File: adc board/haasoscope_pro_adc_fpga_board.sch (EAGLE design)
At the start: 582 parts, among them CN2 12Vin, IC1 ADC12DL2500ACF, IC10 TPS72325DBVR, IC13 LMH5401IRMST, IC14 LMH6401IRMZR, IC15 SN74AVC4T774PWR, IC17 DAC8562SDGSR, IC18 TLV9102IPWR, IC2 SN74AVC4T774PWR, IC21 LMH5401IRMST, IC22 TPS7A7200RGTR, IC23 TPS7A7200RGTR, IC24 TPS7A7200RGTR, IC25 TPS72325DBVR, IC26 TPS7A7200RGTR, IC27 TPS7A7200RGTR, IC28 TPS7A7200RGTR, IC29 LMH6401IRMZR, IC3 ADC122S021CIMM_NOPB, IC30 SN74AVC4T774PWR, IC33 TLV9102IPWR, IC4 TLV9102IPWR, IC5 EP4CE30F23C6N, IC6 EPCQ16ASI8N, IC7 TPS7A7200RGTR, IC8 FT232HQ, IC9 93LC56B, J1 2p-2.54, J10 8pin, J11 8pin, J13 8pin, J15 test1, J2 test1, J3 2p-2.54, J30 2p-2.54, J31 2p-2.54, J32 2p-2.54, J33 2p-2.54, J34 2p-2.54, J35 2p-2.54, J36 2p-2.54, J37 2p-2.54, J39 2p-2.54, J4 2p-2.54, J40 2p-2.54, J41 2p-2.54, J42 2p-2.54, J43 2p-2.54, J44 2p-2.54, J45 2p-2.54, J46 2p-2.54, J8 8pin, K1 G6K-2F-RF-T-TR03_DC5, K2 G6K-2F-RF-T-TR03_DC5, K3 G6K-2F-RF-T-TR03_DC5, K4 G6K-2F-RF-T-TR03_DC5, K5 G6K-2F-RF-T-TR03_DC5, K6 TLP3475R_TP,F, K7 TLP3475R_TP,F, Q1 S8050, Q2 FDN340P, Q4 S8050, Q5 S8050, Q7 S8050, Q8 S8050, Q9 S8050, SW3 SKQGADE010, SW4 SKQGADE010, U2 ADF4350BCPZ, X1 USBC, Y2 OSCILLATORSMD-5X3, Y3 12MHz

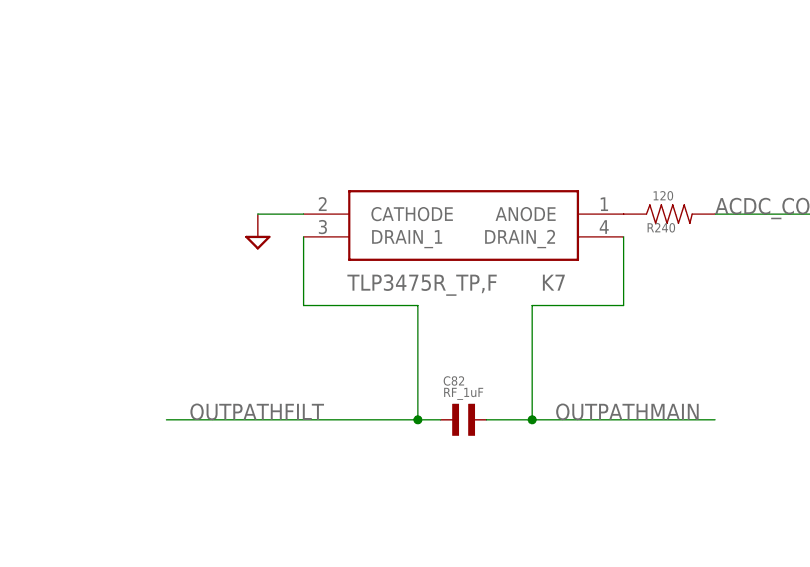
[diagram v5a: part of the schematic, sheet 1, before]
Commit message: 3475R -> 3475 in sch and brd
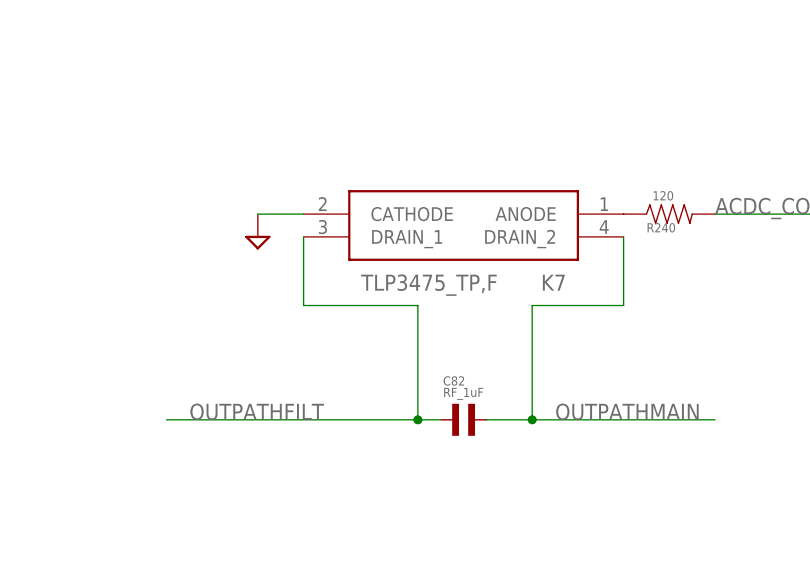
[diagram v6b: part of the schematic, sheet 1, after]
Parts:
- K6, K7: value TLP3475R_TP,F -> TLP3475_TP,F; device TLP3475R_TP_F:TLP3475R_TP,F -> TLP3475_TP_F:TLP3475_TP,F
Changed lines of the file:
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@@
 <part name="SUPPLY18" library="supply2" library_urn="urn:adsk.eagle:library:372" deviceset="GND" device=""/>
 <part name="SUPPLY19" library="supply2" library_urn="urn:adsk.eagle:library:372" deviceset="GND" device=""/>
-<part name="K6" library="TLP3475R_TP_F" deviceset="TLP3475R_TP,F" device="">
+<part name="K6" library="TLP3475_TP_F" deviceset="TLP3475_TP,F" device="">
 <attribute name="MANUFACTURER_PART_NUMBER" value="TLP3475"/>
 <attribute name="MOUSER_PART_NUMBER" value="757-TLP3475"/>
 </part>
 <part name="SUPPLY20" library="supply2" library_urn="urn:adsk.eagle:library:372" deviceset="GND" device=""/>
-<part name="K7" library="TLP3475R_TP_F" deviceset="TLP3475R_TP,F" device="">
+<part name="K7" library="TLP3475_TP_F" deviceset="TLP3475_TP,F" device="">
 <attribute name="MANUFACTURER_PART_NUMBER" value="TLP3475"/>
 <attribute name="MOUSER_PART_NUMBER" value="757-TLP3475"/>

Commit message: working on fpga symbol
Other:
- moved on the sheet: 1KHZOUT50, C59, CLKEXT, CLKOUT2, EXTTRIGIN, J1, R136, R160, R210, R211, R31, U$1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
